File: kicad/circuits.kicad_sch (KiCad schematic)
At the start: 26 parts

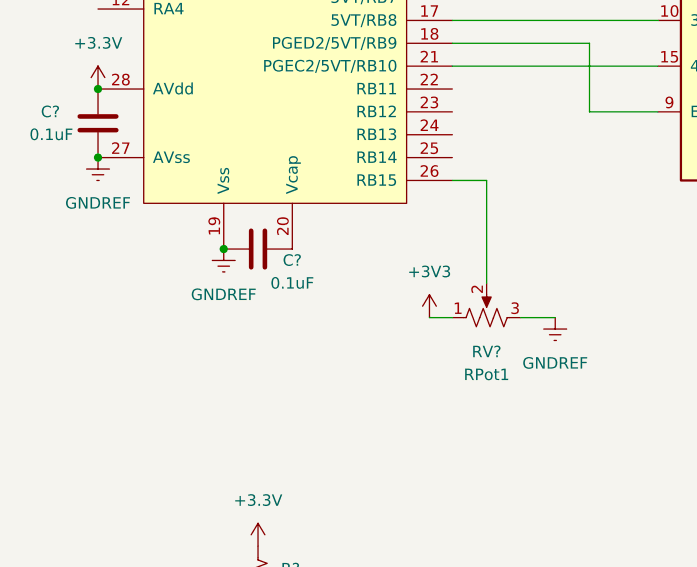
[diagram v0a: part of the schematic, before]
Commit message: Fix cap on circuit schematic
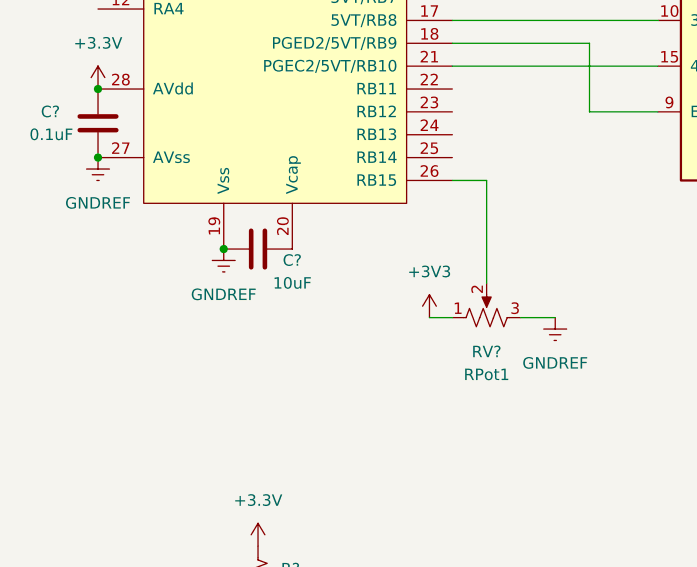
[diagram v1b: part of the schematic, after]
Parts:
- C?: value 0.1uF -> 10uF
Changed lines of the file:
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@@
     (in_bom yes) (on_board yes)
     (property "Reference" "C?" (id 0) (at 63.5 86.36 90))
-    (property "Value" "0.1uF" (id 1) (at 63.5 88.9 90))
+    (property "Value" "10uF" (id 1) (at 63.5 88.9 90))
     (property "Footprint" "" (id 2) (at 63.5 84.1248 0)
       (effects (font (size 1.27 1.27)) hide)
@@
     )
     (path "/1a6f3c8d-1462-4485-be33-8c1fe3f4d604"
-      (reference "C?") (unit 1) (value "0.1uF") (footprint "")
+      (reference "C?") (unit 1) (value "10uF") (footprint "")
     )
     (path "/6957f5cf-e005-4f44-ac03-9d9405342d8f"

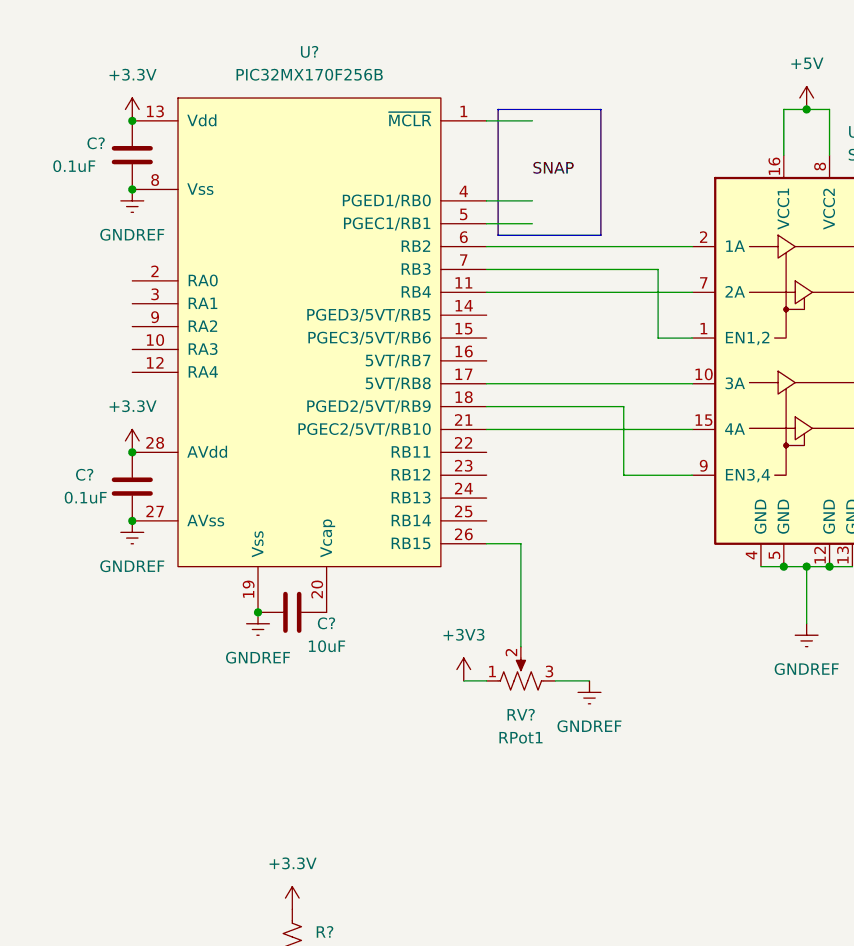
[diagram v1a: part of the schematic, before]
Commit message: Update phase control pins to valid channel pins in schematic
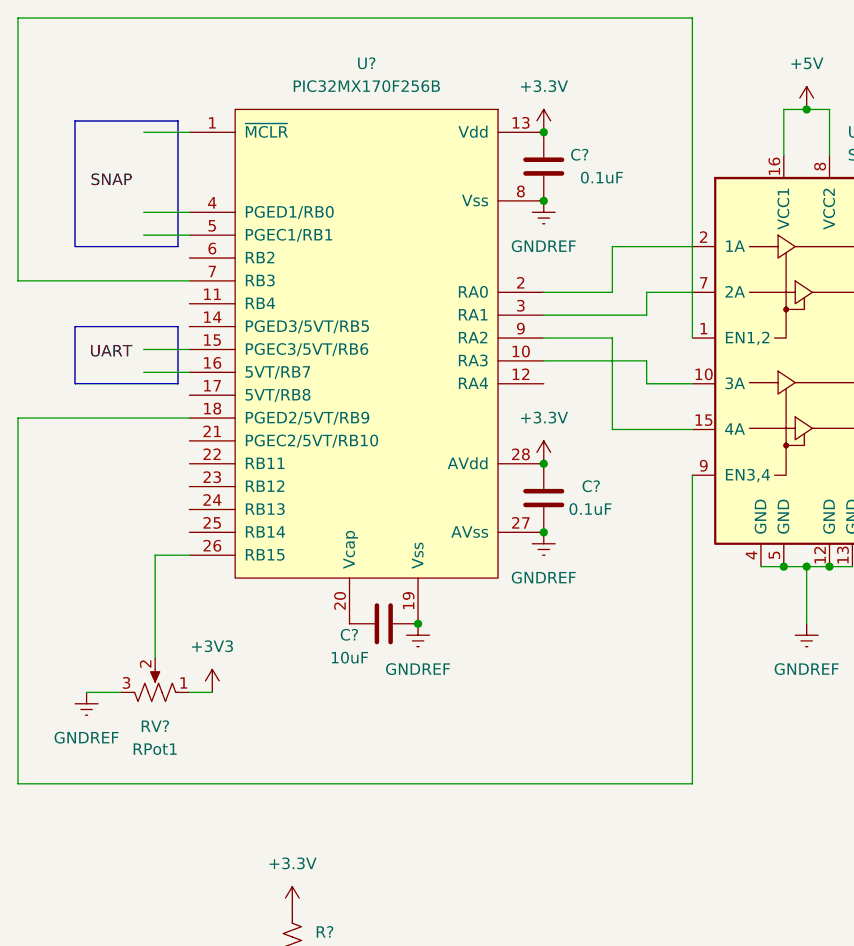
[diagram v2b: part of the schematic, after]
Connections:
- net at U?.10 (RA3): now also U?.10 (3A)
- net at U?.11 (RB4): no longer U?.7 (2A)
- net at U?.17 (5VT/RB8): no longer U?.10 (3A)
- net at U?.2 (RA0): now also U?.2 (1A)
- net at U?.21 (PGEC2/5VT/RB10): no longer U?.15 (4A)
- net at U?.3 (RA1): now also U?.7 (2A)
- net at U?.6 (RB2): no longer U?.2 (1A)
- net at U?.9 (RA2): now also U?.15 (4A)
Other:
- moved on the sheet: C?, RV?, U?

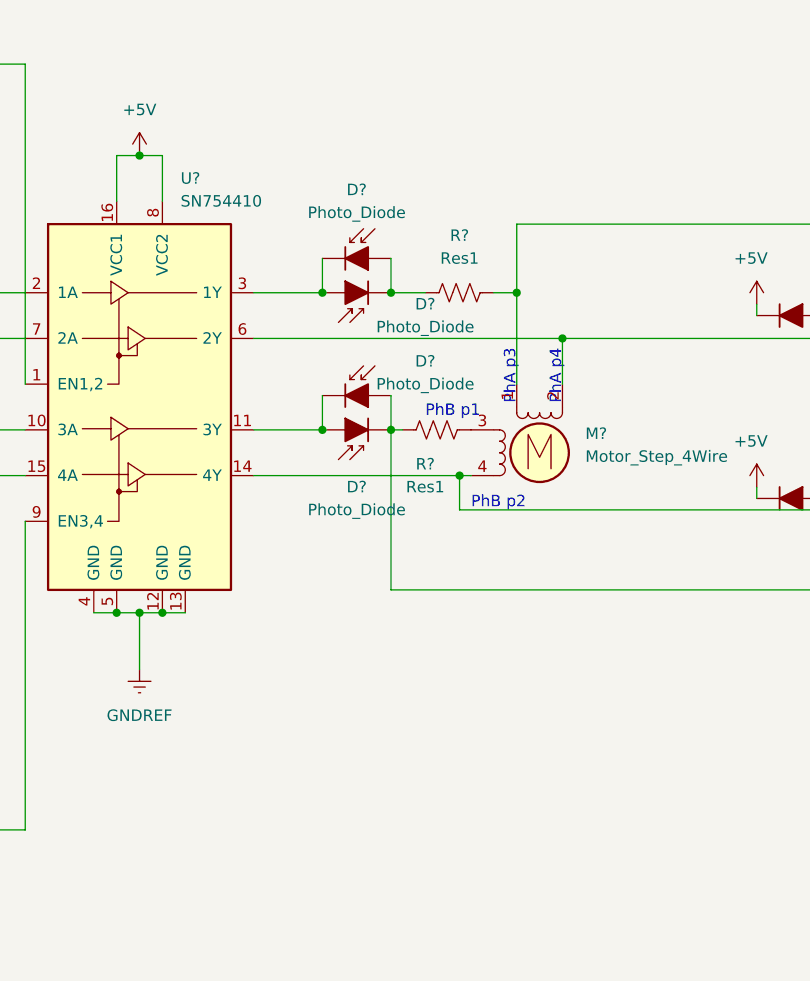
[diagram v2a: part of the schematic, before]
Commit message: [STABLE] Make one phase on work
* Switched timers for PWM to work
* Put LED and current limiting resistor in parallel to each coil, allowing full
3.3V
across the coil
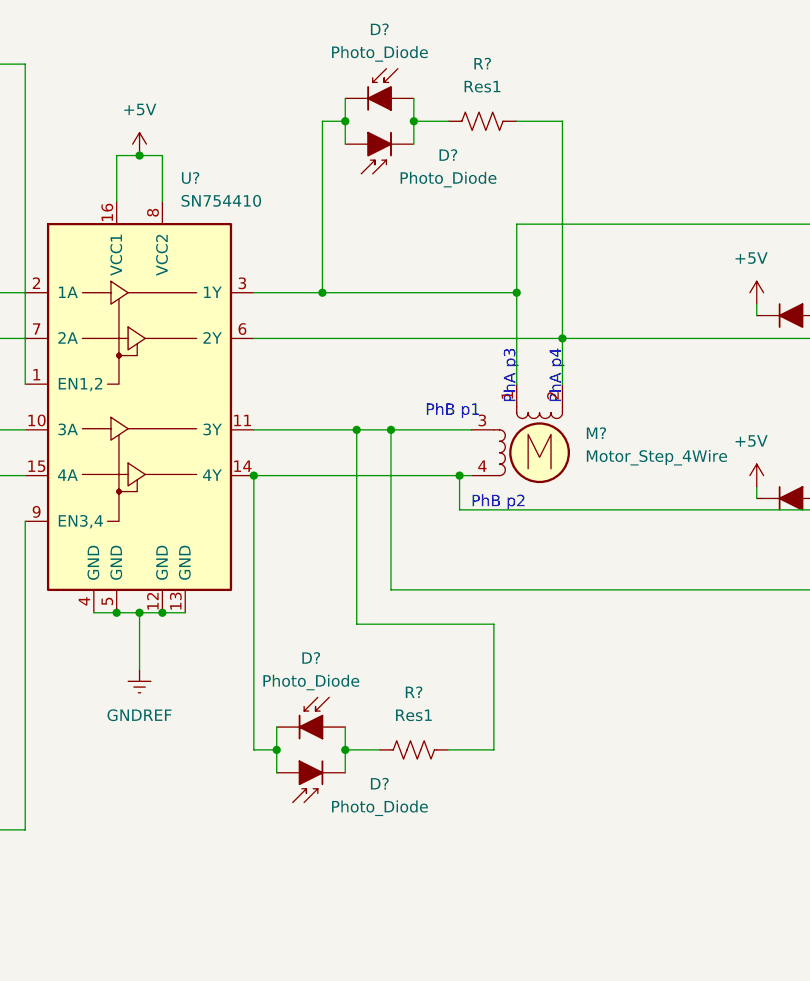
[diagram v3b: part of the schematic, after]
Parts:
- removed D? (x4): Photo_Diode, symbol ME218_BaseLib:Photo_Diode
- removed R? (x2): Res1, symbol ME218_BaseLib:Res1
- added D? (x4): Photo_Diode, symbol ME218_BaseLib:Photo_Diode
- added R? (x2): Res1, symbol ME218_BaseLib:Res1
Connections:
- net at D?.1 (K), D?.2 (A): now also M?.3, U?.11 (3Y), R?.2
- net at D?.1 (K), D?.2 (A), M?.2 (-)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: now also R?.2
- net at U?.3 (1Y): now also D?.1 (K), D?.2 (A), M?.1, D?.1 (K), D?.2 (A)
- net at D?.1 (K), D?.2 (A), M?.4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: now also D?.1 (K), D?.2 (A)
- new net: D?.1 (K), D?.2 (A), R?.1 (x2)

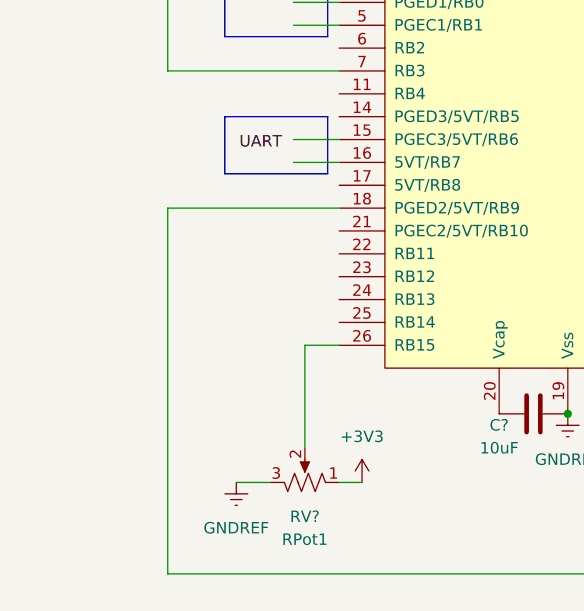
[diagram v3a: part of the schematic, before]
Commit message: Change rotation direction with button
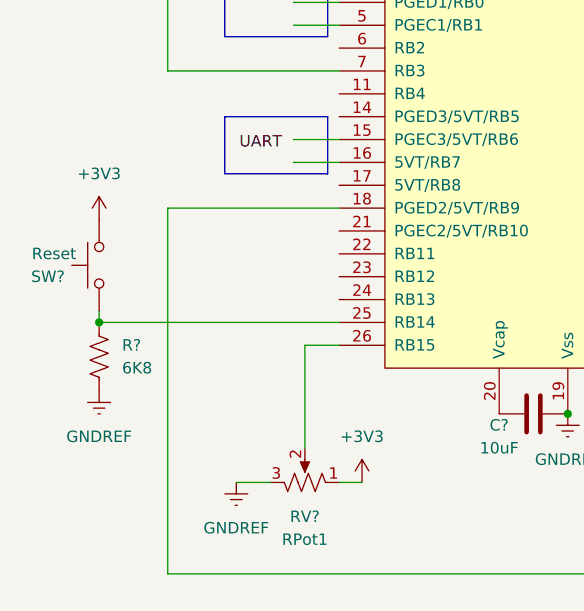
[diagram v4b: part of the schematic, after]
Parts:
- added R?: 6K8, symbol Device:R_US
- added SW?: Reset, symbol ME218_BaseLib:SW-PB
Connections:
- net +3V3: now also SW?.2
- net GNDREF: now also R?.1
- net at U?.25 (RB14): now also R?.2, SW?.1
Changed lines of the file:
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@@
   (junction (at 116.84 29.21) (diameter 0) (color 0 0 0 0)
   )
+  (junction (at 21.59 76.2) (diameter 0) (color 0 0 0 0)
+  )
   (junction (at 87.63 39.37) (diameter 0) (color 0 0 0 0)
   )
@@
     (stroke (width 0) (type default) (color 0 0 0 0))
   )
+  (wire (pts (xy 21.59 74.93) (xy 21.59 76.2))
+    (stroke (width 0) (type default) (color 0 0 0 0))
+  )
   (wire (pts (xy 147.32 25.4) (xy 151.13 25.4))
     (stroke (width 0) (type default) (color 0 0 0 0))
@@
   )
   (wire (pts (xy 158.75 44.45) (xy 158.75 54.61))
+    (stroke (width 0) (type default) (color 0 0 0 0))
+  )
+  (wire (pts (xy 21.59 76.2) (xy 48.26 76.2))
     (stroke (width 0) (type default) (color 0 0 0 0))
   )
@@
     (pin "2")
   )
+  (symbol (lib_id "power:+3V3") (at 21.59 64.77 0) (unit 1)
+    (in_bom yes) (on_board yes) (fields_autoplaced)
+    (property "Reference" "#PWR?" (id 0) (at 21.59 68.58 0)
+      (effects (font (size 1.27 1.27)) hide)
+    )
+    (property "Value" "+3V3" (id 1) (at 21.59 59.69 0))
+    (property "Footprint" "" (id 2) (at 21.59 64.77 0)
+      (effects (font (size 1.27 1.27)) hide)
+    )
+    (property "Datasheet" "" (id 3) (at 21.59 64.77 0)
+      (effects (font (size 1.27 1.27)) hide)
+    )
+    (pin "1")
+  )
+  (symbol (lib_id "ME218_BaseLib:SW-PB") (at 21.59 69.85 90) (unit 1)
+    (in_bom yes) (on_board yes)
+    (property "Reference" "SW?" (id 0) (at 17.78 71.1201 90)
+      (effects (font (size 1.27 1.27)) (justify left))
+    )
+    (property "Value" " Reset" (id 1) (at 19.05 68.58 90)
+      (effects (font (size 1.27 1.27)) (justify left))
+    )
+    (property "Footprint" "" (id 2) (at 16.51 69.85 0)
+      (effects (font (size 1.27 1.27)) hide)
+    )
+    (property "Datasheet" "" (id 3) (at 16.51 69.85 0)
+      (effects (font (size 1.27 1.27)) hide)
+    )
+    (pin "1")
+    (pin "2")
+  )
   (symbol (lib_id "ME218_BaseLib:RPot1") (at 44.45 93.98 270) (mirror x) (unit 1)
     (in_bom yes) (on_board yes) (fields_autoplaced)
@@
     (pin "2")
     (pin "3")
+  )
+  (symbol (lib_id "power:GNDREF") (at 21.59 83.82 0) (unit 1)
+    (in_bom yes) (on_board yes) (fields_autoplaced)
+    (property "Reference" "#PWR?" (id 0) (at 21.59 90.17 0)
+      (effects (font (size 1.27 1.27)) hide)
+    )
+    (property "Value" "GNDREF" (id 1) (at 21.59 88.9 0))
+    (property "Footprint" "" (id 2) (at 21.59 83.82 0)
+      (effects (font (size 1.27 1.27)) hide)
+    )
+    (property "Datasheet" "" (id 3) (at 21.59 83.82 0)
+      (effects (font (size 1.27 1.27)) hide)
+    )
+    (pin "1")
   )
   (symbol (lib_id "ME218_BaseLib:Diode") (at 228.6 67.31 0) (unit 1)
@@
     (pin "2")
   )
+  (symbol (lib_id "Device:R_US") (at 21.59 80.01 180) (unit 1)
+    (in_bom yes) (on_board yes) (fields_autoplaced)
+    (property "Reference" "R?" (id 0) (at 24.13 78.7399 0)
+      (effects (font (size 1.27 1.27)) (justify right))
+    )
+    (property "Value" "6K8" (id 1) (at 24.13 81.2799 0)
+      (effects (font (size 1.27 1.27)) (justify right))
+    )
+    (property "Footprint" "" (id 2) (at 20.574 79.756 90)
+      (effects (font (size 1.27 1.27)) hide)
+    )
+    (property "Datasheet" "~" (id 3) (at 21.59 80.01 0)
+      (effects (font (size 1.27 1.27)) hide)
+    )
+    (pin "1")
+    (pin "2")
+  )
   (symbol (lib_id "power:GNDREF") (at 87.63 76.2 0) (mirror y) (unit 1)
     (in_bom yes) (on_board yes) (fields_autoplaced)
@@
       (reference "#PWR?") (unit 1) (value "+3V3") (footprint "")
     )
+    (path "/2fef238e-9148-49f1-8547-d3c85b4a6e9c"
+      (reference "#PWR?") (unit 1) (value "+3V3") (footprint "")
+    )
+    (path "/3c6bc026-803d-44ce-acdd-bcb0f79dc704"
+      (reference "#PWR?") (unit 1) (value "GNDREF") (footprint "")
+    )
     (path "/4541adf6-bfb4-44d0-8f02-5ba9ff8171f7"
       (reference "#PWR?") (unit 1) (value "GNDREF") (footprint "")
@@
       (reference "R?") (unit 1) (value "Res1") (footprint "")
     )
+    (path "/d4aee8fa-a9d0-42bf-9774-1cb7e39480f9"
+      (reference "R?") (unit 1) (value "6K8") (footprint "")
+    )
     (path "/de19ac5d-6439-4226-b79e-55ad3ef8141f"
       (reference "R?") (unit 1) (value " 10k") (footprint "")
@@
       (reference "RV?") (unit 1) (value "RPot1") (footprint "")
     )
+    (path "/3256e3f8-dfa3-47ce-85fa-89028cc75364"
+      (reference "SW?") (unit 1) (value " Reset") (footprint "")
+    )
     (path "/eb0d2ab4-d10d-41f8-be7c-0e5badacc448"

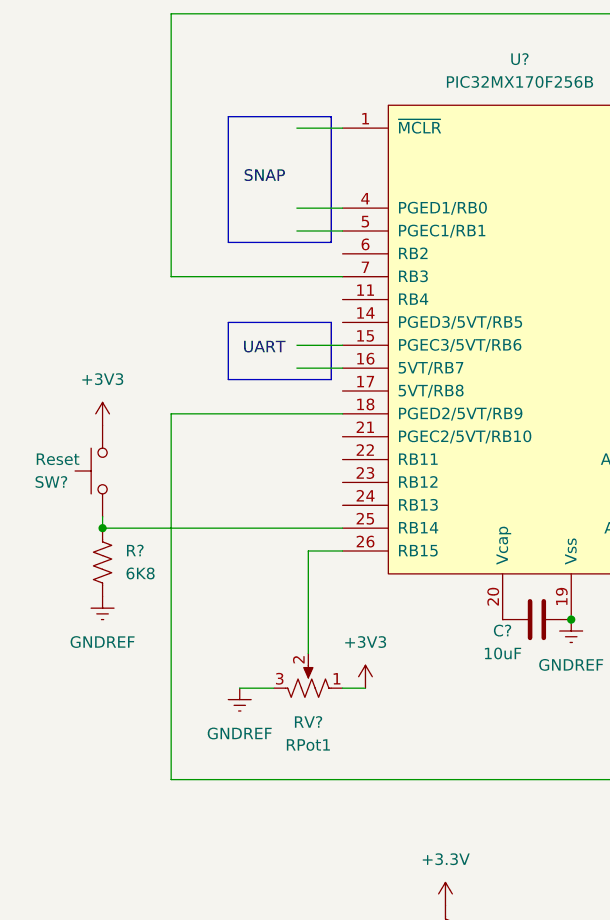
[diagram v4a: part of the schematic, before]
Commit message: Create speed dial service (failing to read dial)
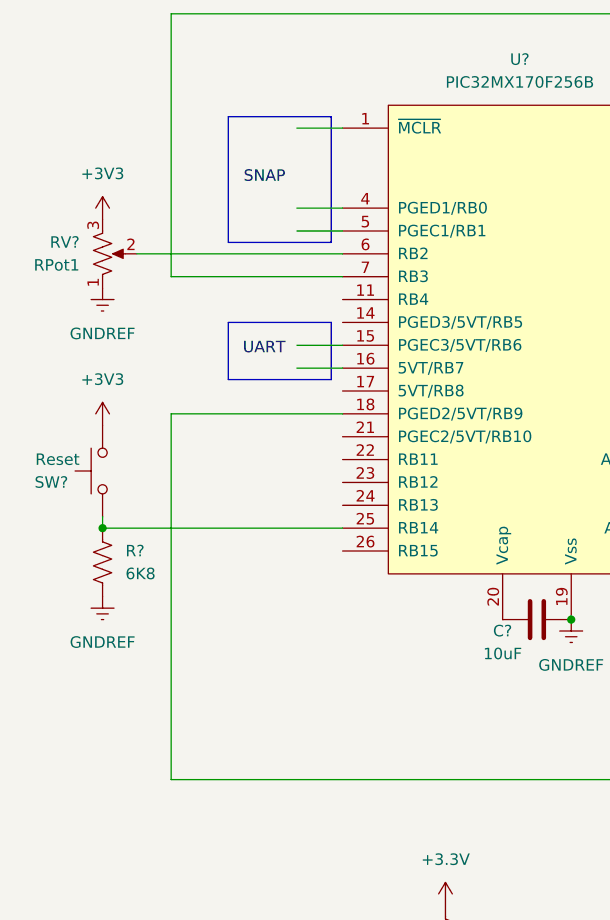
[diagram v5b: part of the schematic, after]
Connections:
- net +3V3: now also RV?.3; no longer RV?.1
- net GNDREF: now also RV?.1; no longer RV?.3
- net at RV?.2: now also U?.6 (RB2); no longer U?.26 (RB15)
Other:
- moved on the sheet: RV?
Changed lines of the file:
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@@
-    (stroke (width 0) (type default) (color 0 0 0 0))
-  )
-  (wire (pts (xy 48.26 78.74) (xy 44.45 78.74))
     (stroke (width 0) (type default) (color 0 0 0 0))
   )
@@
     (stroke (width 0) (type default) (color 0 0 0 0))
   )
-  (wire (pts (xy 50.8 93.98) (xy 48.26 93.98))
-    (stroke (width 0) (type default) (color 0 0 0 0))
-  )
   (wire (pts (xy 88.9 154.94) (xy 110.49 154.94))
     (stroke (width 0) (type default) (color 0 0 0 0))
@@
     (stroke (width 0) (type default) (color 0 0 0 0))
   )
-  (wire (pts (xy 40.64 93.98) (xy 36.83 93.98))
+  (wire (pts (xy 25.4 45.72) (xy 48.26 45.72))
     (stroke (width 0) (type default) (color 0 0 0 0))
   )
@@
   )
   (wire (pts (xy 144.78 59.69) (xy 153.67 59.69))
-    (stroke (width 0) (type default) (color 0 0 0 0))
-  )
-  (wire (pts (xy 44.45 78.74) (xy 44.45 90.17))
     (stroke (width 0) (type default) (color 0 0 0 0))
   )
@@
     (pin "2")
   )
-  (symbol (lib_id "ME218_BaseLib:RPot1") (at 44.45 93.98 270) (mirror x) (unit 1)
-    (in_bom yes) (on_board yes) (fields_autoplaced)
-    (property "Reference" "RV?" (id 0) (at 44.45 97.79 90))
-    (property "Value" "RPot1" (id 1) (at 44.45 100.33 90))
-    (property "Footprint" "" (id 2) (at 44.45 93.98 0)
-      (effects (font (size 1.27 1.27)) hide)
-    )
-    (property "Datasheet" "" (id 3) (at 44.45 93.98 0)
+  (symbol (lib_id "ME218_BaseLib:RPot1") (at 21.59 45.72 0) (mirror x) (unit 1)
+    (in_bom yes) (on_board yes) (fields_autoplaced)
+    (property "Reference" "RV?" (id 0) (at 19.05 44.4499 0)
+      (effects (font (size 1.27 1.27)) (justify right))
+    )
+    (property "Value" "RPot1" (id 1) (at 19.05 46.9899 0)
+      (effects (font (size 1.27 1.27)) (justify right))
+    )
+    (property "Footprint" "" (id 2) (at 21.59 45.72 0)
+      (effects (font (size 1.27 1.27)) hide)
+    )
+    (property "Datasheet" "" (id 3) (at 21.59 45.72 0)
       (effects (font (size 1.27 1.27)) hide)
     )
@@
     (pin "9")
   )
-  (symbol (lib_id "power:+3V3") (at 50.8 93.98 0) (mirror y) (unit 1)
-    (in_bom yes) (on_board yes) (fields_autoplaced)
-    (property "Reference" "#PWR?" (id 0) (at 50.8 97.79 0)
-      (effects (font (size 1.27 1.27)) hide)
-    )
-    (property "Value" "+3V3" (id 1) (at 50.8 88.9 0))
-    (property "Footprint" "" (id 2) (at 50.8 93.98 0)
-      (effects (font (size 1.27 1.27)) hide)
-    )
-    (property "Datasheet" "" (id 3) (at 50.8 93.98 0)
-      (effects (font (size 1.27 1.27)) hide)
-    )
-    (pin "1")
-  )
-  (symbol (lib_id "power:GNDREF") (at 36.83 93.98 0) (mirror y) (unit 1)
-    (in_bom yes) (on_board yes) (fields_autoplaced)
-    (property "Reference" "#PWR?" (id 0) (at 36.83 100.33 0)
-      (effects (font (size 1.27 1.27)) hide)
-    )
-    (property "Value" "GNDREF" (id 1) (at 36.83 99.06 0))
-    (property "Footprint" "" (id 2) (at 36.83 93.98 0)
-      (effects (font (size 1.27 1.27)) hide)
-    )
-    (property "Datasheet" "" (id 3) (at 36.83 93.98 0)
-      (effects (font (size 1.27 1.27)) hide)
-    )
+  (symbol (lib_id "power:+3V3") (at 21.59 41.91 0) (mirror y) (unit 1)
+    (in_bom yes) (on_board yes) (fields_autoplaced)
+    (property "Reference" "#PWR?" (id 0) (at 21.59 45.72 0)
+      (effects (font (size 1.27 1.27)) hide)
+    )
+    (property "Value" "+3V3" (id 1) (at 21.59 36.83 0))
+    (property "Footprint" "" (id 2) (at 21.59 41.91 0)
+      (effects (font (size 1.27 1.27)) hide)
+    )
+    (property "Datasheet" "" (id 3) (at 21.59 41.91 0)
+      (effects (font (size 1.27 1.27)) hide)
+    )
+    (pin "1")
+  )
+  (symbol (lib_id "power:GNDREF") (at 21.59 49.53 0) (mirror y) (unit 1)
+    (in_bom yes) (on_board yes) (fields_autoplaced)
+    (property "Reference" "#PWR?" (id 0) (at 21.59 55.88 0)
+      (effects (font (size 1.27 1.27)) hide)
+    )
+    (property "Value" "GNDREF" (id 1) (at 21.59 54.61 0))
+    (property "Footprint" "" (id 2) (at 21.59 49.53 0)
+      (effects (font (size 1.27 1.27)) hide)
+    )
+    (property "Datasheet" "" (id 3) (at 21.59 49.53 0)
+      (effects (font (size 1.27 1.27)) hide)
+    )
